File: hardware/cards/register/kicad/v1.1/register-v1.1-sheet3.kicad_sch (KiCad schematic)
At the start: 10 parts, among them IC19 74*192, IC20 74*192, IC21 74*192, IC22 74*192, IC23 74*244, IC24 74*244, IC25 74*32, IC26 74*32, IC27 74*244, IC28 74*244

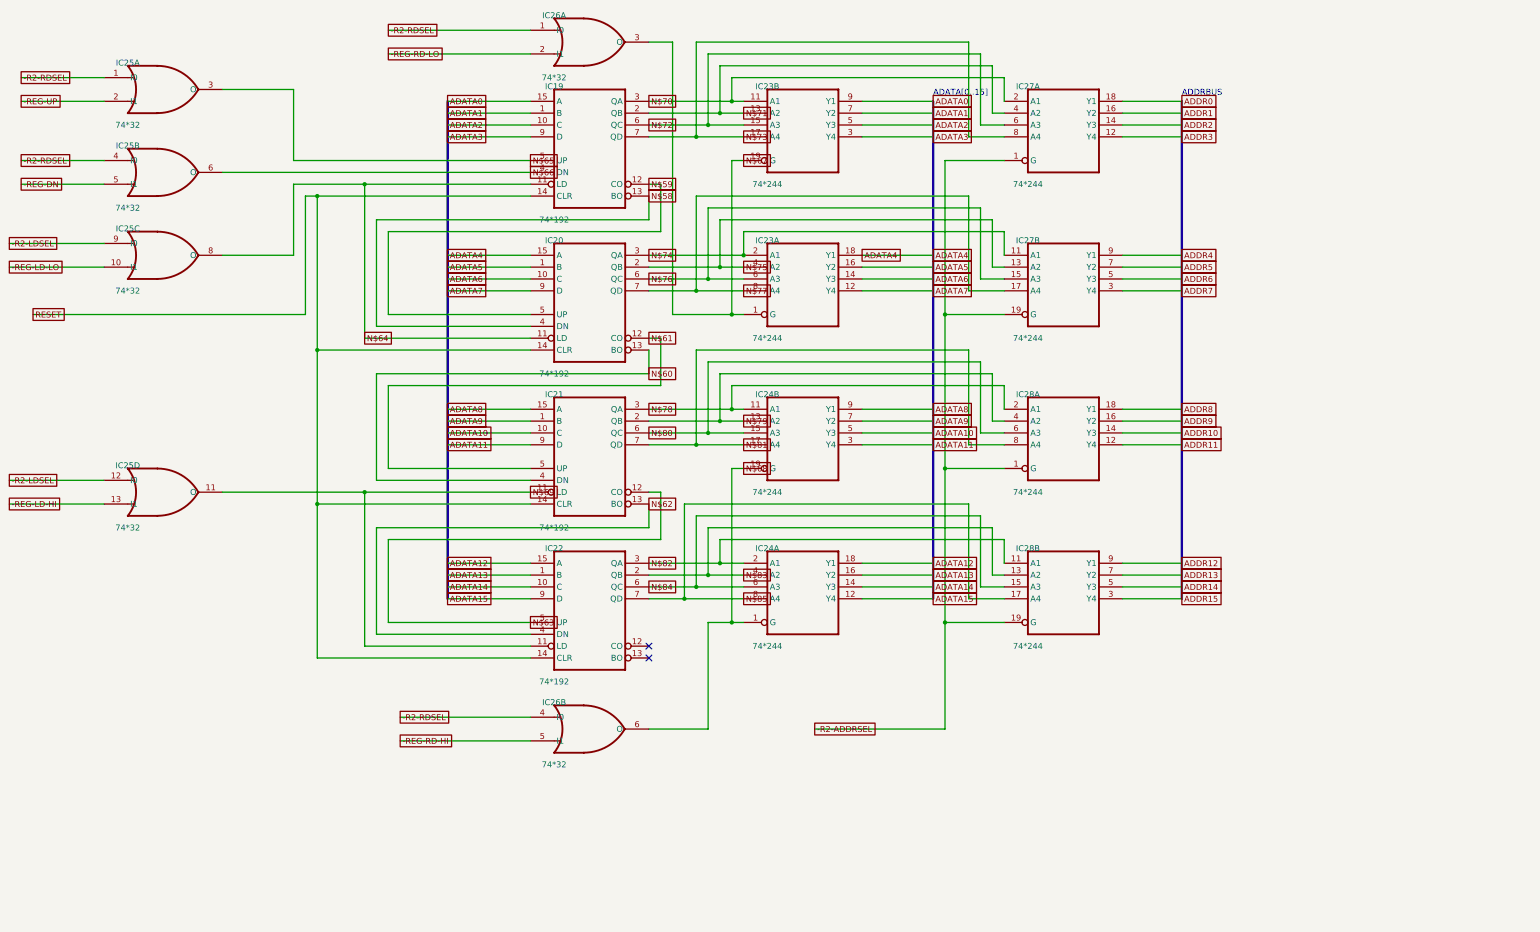
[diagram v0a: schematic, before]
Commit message: fix(kicad): readable converted schematics - overlaps 42,847 -> 3,147, nothing off the frame; CF sheet 0 overlaps
- tools/kicad/sch_overlaps.py: calibrated readability check (text/text, text/body, text/line, off frame/title block)
- eagle_sch_to_kicad.py: fields placed from Eagle's smashed attributes or the symbol's >NAME/>VALUE with Eagle's align,
  size and ratio, readable angles; fields Eagle never shows hidden (FABC96R shows only its pin name); pin numbers hidden
  where every Eagle pin hides them; Eagle-hidden layers dropped (the stray SpiceOrder text); labels on their own wires,
  converter labels only where KiCad needs them; rotate-then-mirror fixed for MR90/MR270 in pin_world/no-connects;
  each sheet on the smallest page that holds it, centred clear of the title block
- finish_board.py: stable footprint-library choice (DRC counts no longer vary run to run)
- all 37 projects regenerated: netlist proofs unchanged (34 MATCH, 2 schematic-only, video Fusion export MISMATCH as
  before); DRC same or better; ERC up (loose wire ends onto graphic buses no longer hidden by labels; explained per README)
- CF card: gate names off the gate bodies, U3 clear of its title, 5.08 mm connector pins; rebuilt: DRC 0/0, proof MATCH
- schematic PDFs regenerated (tools/sch_to_pdf.py, 37/37)

Co-Authored-By: Claude Opus 5.5 <noreply@anthropic.com>
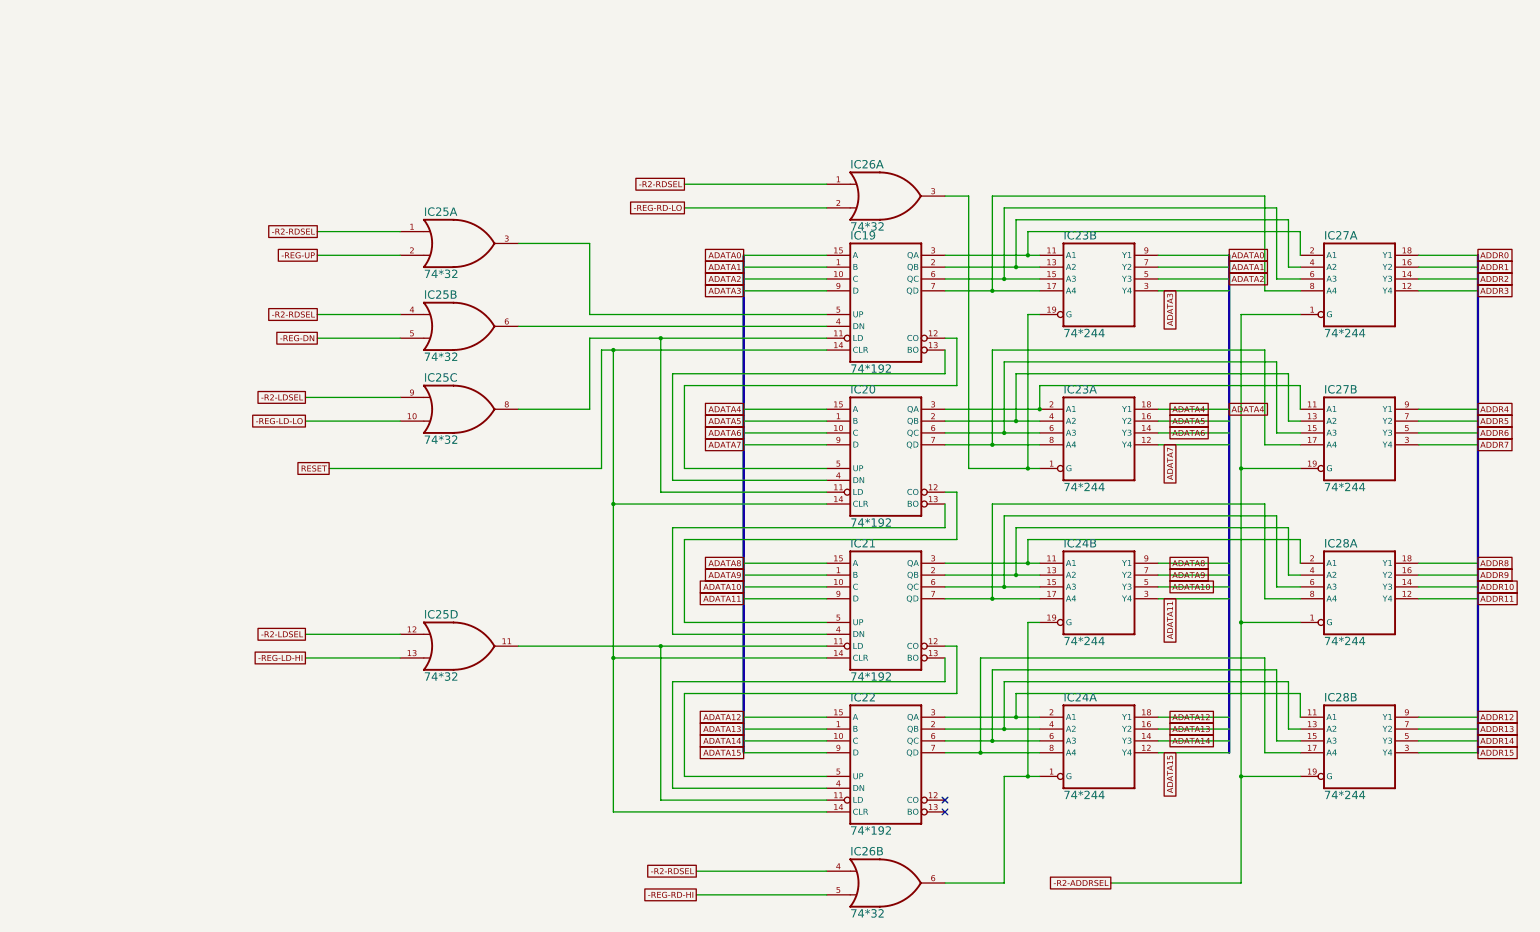
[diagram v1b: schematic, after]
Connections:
- net N$58: no longer names the net of IC19.13 (BO), IC20.4 (DN)
- net N$59: no longer names the net of IC19.12 (CO), IC20.5 (UP)
- net N$60: no longer names the net of IC20.13 (BO), IC21.4 (DN)
- net N$61: no longer names the net of IC20.12 (CO), IC21.5 (UP)
- net N$62: no longer names the net of IC21.13 (BO), IC22.4 (DN)
- net N$63: no longer names the net of IC21.12 (CO), IC22.5 (UP)
- net N$64: no longer names the net of IC19.11 (LD), IC20.11 (LD), IC25.8 (O)
- net N$65: no longer names the net of IC19.5 (UP), IC25.3 (O)
- net N$66: no longer names the net of IC19.4 (DN), IC25.6 (O)
- net N$67: no longer names the net of IC23.1 (G), IC23.19 (G), IC26.3 (O)
- net N$68: no longer names the net of IC24.1 (G), IC24.19 (G), IC26.6 (O)
- net N$69: no longer names the net of IC21.11 (LD), IC22.11 (LD), IC25.11 (O)
- net N$70: no longer names the net of IC19.3 (QA), IC23.11 (A1), IC27.2 (A1)
- net N$71: no longer names the net of IC19.2 (QB), IC23.13 (A2), IC27.4 (A2)
- net N$72: no longer names the net of IC19.6 (QC), IC23.15 (A3), IC27.6 (A3)
- net N$73: no longer names the net of IC19.7 (QD), IC23.17 (A4), IC27.8 (A4)
- net N$74: no longer names the net of IC20.3 (QA), IC23.2 (A1), IC27.11 (A1)
- net N$75: no longer names the net of IC20.2 (QB), IC23.4 (A2), IC27.13 (A2)
- net N$76: no longer names the net of IC20.6 (QC), IC23.6 (A3), IC27.15 (A3)
- net N$77: no longer names the net of IC20.7 (QD), IC23.8 (A4), IC27.17 (A4)
- net N$78: no longer names the net of IC21.3 (QA), IC24.11 (A1), IC28.2 (A1)
- net N$79: no longer names the net of IC21.2 (QB), IC24.13 (A2), IC28.4 (A2)
- net N$80: no longer names the net of IC21.6 (QC), IC24.15 (A3), IC28.6 (A3)
- net N$81: no longer names the net of IC21.7 (QD), IC24.17 (A4), IC28.8 (A4)
- net N$82: no longer names the net of IC22.3 (QA), IC24.2 (A1), IC28.11 (A1)
- net N$83: no longer names the net of IC22.2 (QB), IC24.4 (A2), IC28.13 (A2)
- net N$84: no longer names the net of IC22.6 (QC), IC24.6 (A3), IC28.15 (A3)
- net N$85: no longer names the net of IC22.7 (QD), IC24.8 (A4), IC28.17 (A4)
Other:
- note removed: "ADATA[0..15]"
- note removed: "ADDRBUS"
- moved on the sheet: IC19, IC20, IC21, IC22, IC23A, IC23B, IC24A, IC24B, IC27A, IC27B, IC28A, IC28B
